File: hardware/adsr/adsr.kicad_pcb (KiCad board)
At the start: 4 copper layers, 29 x 100 mm, 88 parts, among them J1 MonoJack, J2 MonoJack, J3 MonoJack, J4 Conn_02x05_Odd_Even, Q1 BC847, Q2 BC847, Q3 BC847, Q4 BC847, Q5 BC847, Q6 BC847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

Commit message: routed PCB, needs cleanup
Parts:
- removed D3: 1N4148, Diode_SMD:D_SOD-123
- C10, U1, U3: moved to B.Cu
- RV1, RV2, RV3, RV4, RV5: footprint Potentiometer_THT:Potentiometer_Bourns_PTV09A-1_Single_Vertical -> Audio_Potentiometer_THT:Potentiometer_Bourns_PTV09A-1_Single_Vertical_thin
- moved C4 105.7 mm to (126.9, 63.4), turned to -90 degrees
- moved C2 91.5 mm to (126.7, 68.4), turned to -90 degrees
- moved C9 89.1 mm to (122.7, 73.2), turned to 90 degrees
- moved R29 87.5 mm to (123.5, 77.7), turned to 0 degrees
- moved U1 86.1 mm to (121.1, 68.2)
- moved D4 78.2 mm to (112.3, 133.3), turned to 90 degrees
- moved R20 77.8 mm to (113.7, 87.0), turned to 180 degrees
- moved R19 76.3 mm to (127.8, 125.4), turned to 90 degrees
- moved R21 74.3 mm to (113.5, 93.2), turned to 180 degrees
- moved Q5 73.3 mm to (127.2, 115.4), turned to 90 degrees
- moved Q7 73.1 mm to (113.6, 90.1), turned to 90 degrees
- moved D6 70.3 mm to (124.1, 123.3), turned to 180 degrees
- moved R25 69.6 mm to (106.4, 95.3), turned to 180 degrees
- moved R26 69.1 mm to (108.4, 97.3), turned to 180 degrees
- moved R16 68.4 mm to (124.6, 121.0)
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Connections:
- net Net-(D4-A) renamed /NTRIG
- C8 pad 1: Net-(D9-K) -> /THR
- D4 pad 1: Net-(D3-K) -> Net-(D4-K)
- D9 pad 2: Net-(D9-A) -> /QOUT
- Q1 pad 3: Net-(D3-K) -> Net-(D4-K)
- R17 pad 2: Net-(SW2B-A) -> Net-(SW2A-C)
- R21 pad 2: Net-(R21-Pad2) -> /ENDOF
- R22 pad 2: Net-(U3-Q) -> /QOUT
- R23 pad 1: Net-(U4C-+) -> Net-(U4D-+)
- R23 pad 2: Net-(R21-Pad2) -> /ENDOF
- R25 pad 1: Net-(U4C-+) -> Net-(U4D-+)
- R26 pad 2: Net-(U4C-+) -> Net-(U4D-+)
- R28 pad 1: Net-(U3-Q) -> Net-(D9-K)
- R7 pad 1: Net-(SW2A-C) -> Net-(SW2B-A)
- R8 pad 1: Net-(D3-A) -> Net-(D4-K)
- RV3 pad 3: Net-(D9-A) -> /THR
- RV4 pad 3: Net-(D9-K) -> /THR
- RV5 pad 3: Net-(D9-K) -> /THR
- SW2 pad 1: Net-(D2-K) -> Net-(Q7-C)
- SW2 pad 2: Net-(Q2-B) -> Net-(SW2A-B)
- SW2 pad 5: Net-(SW2B-B) -> Net-(Q2-B)
- SW2 pad 6: Net-(Q7-C) -> Net-(D2-K)
- U1 pad 2: Net-(SW2B-B) -> Net-(SW2A-B)
- U2 pad 6: Net-(D3-A) -> Net-(D4-K)
- U3 pad 3: Net-(U3-Q) -> /QOUT
- U3 pad 6: Net-(D9-K) -> /THR
- U4 pad 10: Net-(U4C-+) -> /NRESET
- U4 pad 12: /NRESET -> Net-(U4D-+)
- U4 pad 13: Net-(D7-A) -> Net-(Q9-B)
- U4 pad 14: Net-(D7-K) -> /ENDOF
- U4 pad 3: Net-(D9-K) -> /THR
- U4 pad 8: Net-(R21-Pad2) -> Net-(D7-K)
- U4 pad 9: Net-(Q9-B) -> Net-(D7-A)
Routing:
- net /THR: track 0.00 -> 80.3 mm, vias 0 -> 1
- net Net-(D8-A): track 0.00 -> 72.9 mm, vias 0 -> 2
- net Net-(D7-A): track 0.00 -> 45.6 mm, vias 0 -> 2
- net /NRESET: track 0.00 -> 43.0 mm, vias 0 -> 2
- net /NTRIG: track 0.00 -> 41.9 mm, vias 0 -> 2
- net Net-(D2-K): track 0.00 -> 40.3 mm
- net -12V: track 13.5 -> 53.6 mm, vias 0 -> 1
- net Net-(U1-DIS): track 0.00 -> 39.3 mm
- net Net-(D9-K): track 0.00 -> 38.0 mm, vias 0 -> 2
- net Net-(D4-K): track 0.00 -> 34.5 mm, vias 0 -> 2
- net Net-(Q3-C): track 0.00 -> 33.7 mm, vias 0 -> 2
- net Net-(Q9-B): track 0.00 -> 32.0 mm, vias 0 -> 4
- net Net-(Q8-S): track 0.00 -> 31.1 mm, vias 0 -> 2
- net Net-(U4B-+): track 0.00 -> 28.1 mm, vias 0 -> 1
- net Net-(SW2B-A): track 0.00 -> 26.0 mm
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- added copper zone on In1.Cu, net +12V
- removed copper zone on F.Cu, net GND

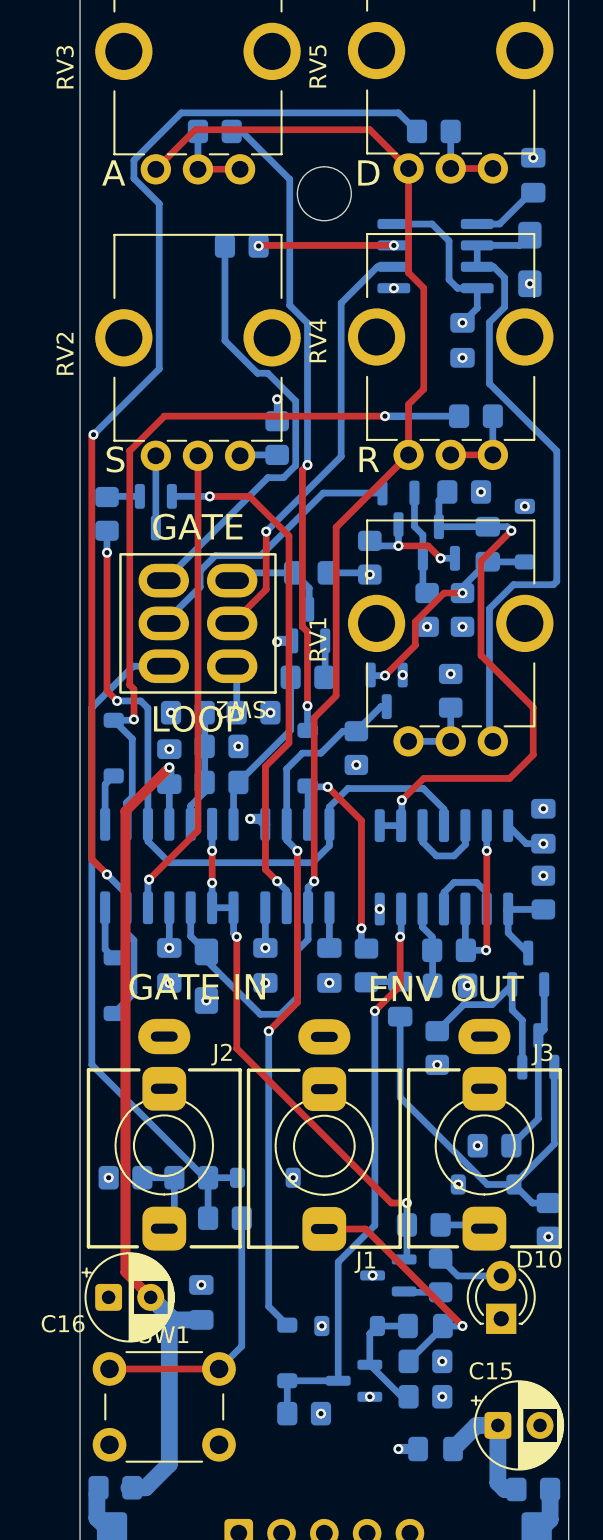
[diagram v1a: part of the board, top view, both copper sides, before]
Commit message: routing cleanup
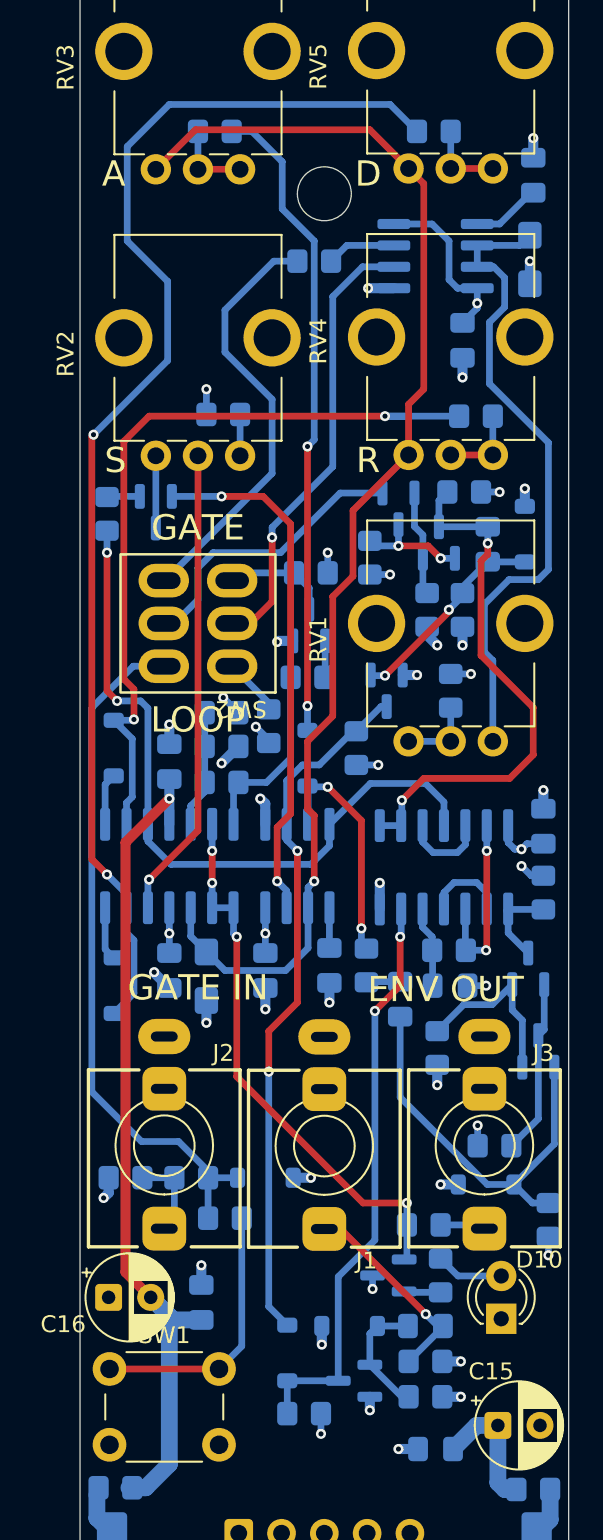
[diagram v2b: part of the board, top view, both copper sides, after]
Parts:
- moved R7 4.39 mm to (113.9, 68.5)
- moved R27 3.49 mm to (108.5, 77.6), turned to 0 degrees
- moved R25 2.00 mm to (108.4, 95.3), turned to 0 degrees
- moved R17 1.20 mm to (111.2, 96.1), turned to 90 degrees
- moved C10 0.30 mm to (111.0, 110.6)
- moved C11 0.30 mm to (105.3, 110.6)
- moved C12 0.30 mm to (105.3, 98.2)
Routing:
- net GND: track 3.17 -> 33.8 mm
- net +12V: track 29.4 -> 43.8 mm, vias 17 -> 18
- net Net-(U1-Q): track 8.04 -> 4.11 mm, vias 2 -> 0
- net /THR: track 80.3 -> 76.8 mm
- net -12V: track 53.6 -> 51.1 mm
- net Net-(C1-Pad2): track 14.8 -> 12.5 mm
- net Net-(D8-A): track 72.9 -> 74.7 mm
- net Net-(Q3-C): track 33.7 -> 31.9 mm
- net Net-(SW2A-B): track 25.8 -> 27.0 mm
- net Net-(D2-K): track 40.3 -> 41.5 mm
- net Net-(SW2A-C): track 2.87 -> 4.02 mm
- net Net-(Q9-B): track 32.0 -> 32.9 mm
- net /ENDOF: track 10.1 -> 11.1 mm
- net Net-(D7-A): track 45.6 -> 46.5 mm
- net Net-(D5-K): track 13.0 -> 12.4 mm
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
